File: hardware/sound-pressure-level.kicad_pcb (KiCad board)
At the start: 2 copper layers, 25 x 25 mm, 33 parts, among them P1 CON-SENSOR2, P2 BOOT, P3 DEBUG, U1 XMC1XXX48, U2 DRILL, U3 DRILL, U4 DRILL, U5 DRILL, U6 ICS-43432, X1 16MHz

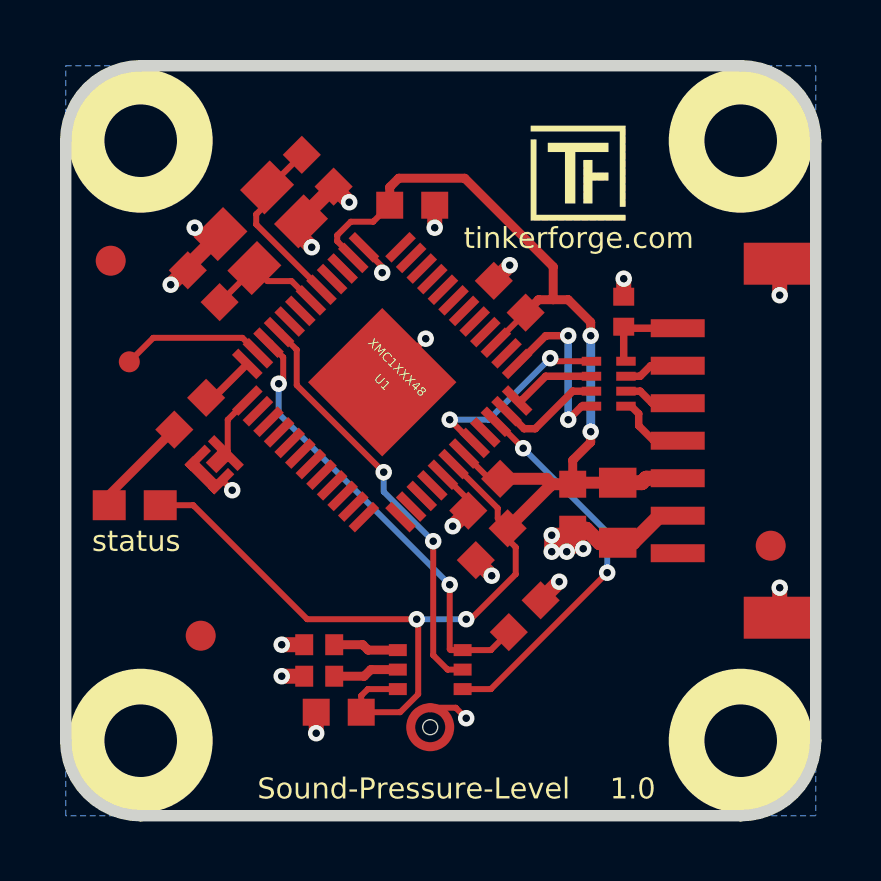
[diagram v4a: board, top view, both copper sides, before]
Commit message: center microphone, pulldown 100k
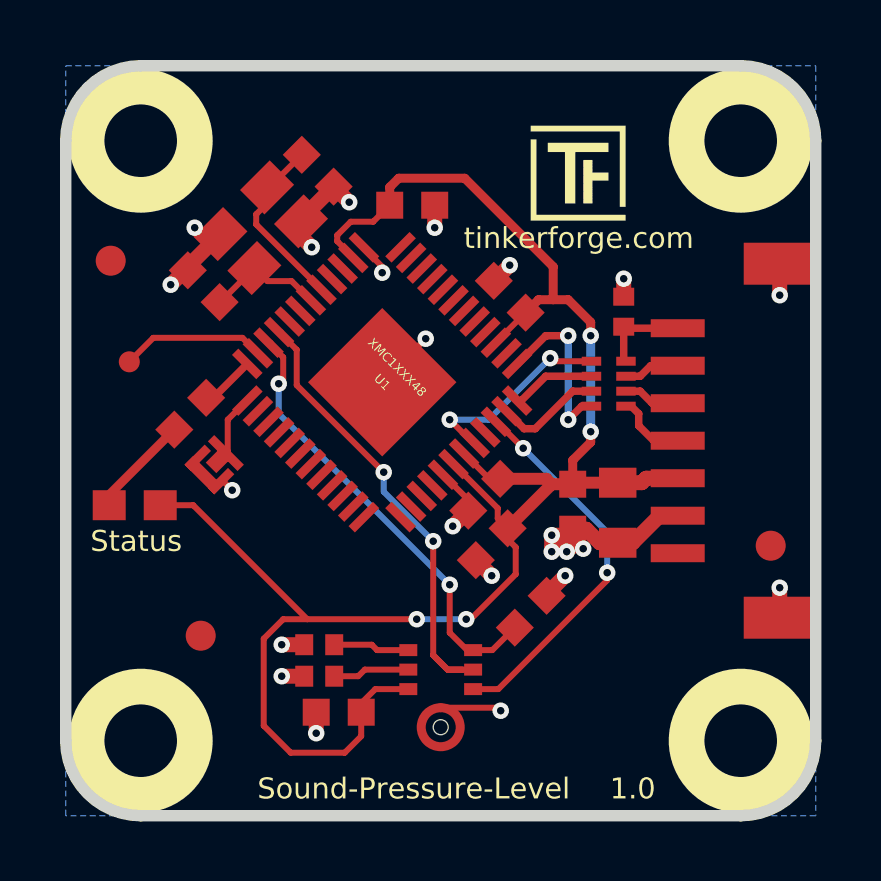
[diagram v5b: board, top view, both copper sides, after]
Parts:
- R2: value 47k -> 100k
- moved U6 0.35 mm to (142.6, 150.6)
- moved R2 0.25 mm to (145.6, 146.7)
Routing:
- net VCC: track 56.5 -> 61.4 mm
- net SCK: track 14.2 -> 15.7 mm
- net GND: track 32.4 -> 33.1 mm
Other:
- board text added: "Status"
- board text removed: "status"
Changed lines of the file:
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@@
-(kicad_pcb (version 4) (host pcbnew 4.0.2+dfsg1-stable)
+(kicad_pcb (version 4) (host pcbnew 4.0.7-e2-6376~58~ubuntu17.04.1)
   (general
     (links 61)
     (no_connects 0)
-    (area 129.909499 128.309499 155.290501 153.690501)
+    (area 13.96714 127.644999 155.955001 196.045)
     (thickness 1.6)
     (drawings 13)
-    (tracks 251)
+    (tracks 257)
     (zones 0)
     (modules 33)
@@
   (layers
     (0 F.Cu signal)
-    (31 B.Cu signal)
+    (31 B.Cu signal hide)
     (32 B.Adhes user)
     (33 F.Adhes user)
@@
     (pad_to_mask_clearance 0)
     (aux_axis_origin 0 0)
-    (visible_elements FFFF7F7F)
+    (visible_elements FFFFFF7F)
     (pcbplotparams
       (layerselection 0x00010_00000000)
@@
   )
   (module kicad-libraries:R0603F (layer F.Cu)
-    (at 145.4 146.85 45)
+    (at 145.6 146.7 45)
     (attr smd)
     (fp_text reference R2 (at 0.05 0.225 45) (layer F.Fab)
       (effects (font (size 0.2 0.2) (thickness 0.05)))
     )
-    (fp_text value 47k (at 0.05 -0.375 45) (layer F.Fab)
+    (fp_text value 100k (at 0.05 -0.375 45) (layer F.Fab)
       (effects (font (size 0.2 0.2) (thickness 0.05)))
     )
@@
   )
   (module kicad-libraries:ICS-43432 (layer F.Cu)
-    (at 142.25 150.55 270)
+    (at 142.6 150.55 270)
     (fp_text reference U6 (at -1.8 0.16 270) (layer F.Fab)
       (effects (font (size 0.15 0.15) (thickness 0.0375)))
@@
     (effects (font (size 0.7 0.7) (thickness 0.15)))
   )
-  (gr_text status (at 132.45 144.35) (layer F.SilkS)
+  (gr_text Status (at 132.45 144.35) (layer F.SilkS)
     (effects (font (size 0.7 0.7) (thickness 0.15)))
   )
@@
   (gr_arc (start 152.6 151) (end 155.1 151) (angle 90) (layer Edge.Cuts) (width 0.381))
   (gr_arc (start 152.6 131) (end 152.6 128.5) (angle 90) (layer Edge.Cuts) (width 0.381))
+  (segment (start 142.6 149.9) (end 144.5 149.9) (width 0.2) (layer F.Cu) (net 1))
+  (via (at 144.6 150) (size 0.55) (drill 0.25) (layers F.Cu B.Cu) (net 1))
+  (segment (start 144.5 149.9) (end 144.6 150) (width 0.2) (layer F.Cu) (net 1))
   (segment (start 134.696447 142.153553) (end 134.696447 142.146447) (width 0.2) (layer F.Cu) (net 1))
   (segment (start 134.696447 142.146447) (end 134.4 141.85) (width 0.2) (layer F.Cu) (net 1))
@@
   (segment (start 138.45 150.05) (end 138.45 150.75) (width 0.5) (layer F.Cu) (net 1))
   (via (at 138.45 150.75) (size 0.55) (drill 0.25) (layers F.Cu B.Cu) (net 1))
-  (segment (start 145.93033 146.31967) (end 146.55 145.7) (width 0.5) (layer F.Cu) (net 1))
-  (via (at 146.55 145.7) (size 0.55) (drill 0.25) (layers F.Cu B.Cu) (net 1))
-  (segment (start 142.25 149.9) (end 143.1 149.9) (width 0.2) (layer F.Cu) (net 1))
-  (via (at 143.45 150.25) (size 0.55) (drill 0.25) (layers F.Cu B.Cu) (net 1))
-  (segment (start 143.1 149.9) (end 143.45 150.25) (width 0.2) (layer F.Cu) (net 1))
+  (segment (start 146.13033 146.11967) (end 146.75 145.5) (width 0.5) (layer F.Cu) (net 1))
+  (via (at 146.75 145.5) (size 0.55) (drill 0.25) (layers F.Cu B.Cu) (net 1))
   (segment (start 146.8 144.15) (end 146.3 144.15) (width 0.5) (layer F.Cu) (net 1))
   (via (at 146.3 144.15) (size 0.55) (drill 0.25) (layers F.Cu B.Cu) (net 1))
@@
   (segment (start 137.943446 133.688066) (end 137.943446 133.617214) (width 0.2) (layer F.Cu) (net 1))
   (segment (start 137.943446 133.617214) (end 139.03033 132.53033) (width 0.5) (layer F.Cu) (net 1))
+  (segment (start 139.95 150.05) (end 139.95 150.85) (width 0.2) (layer F.Cu) (net 2))
+  (segment (start 137.35 146.95) (end 138.15 146.95) (width 0.2) (layer F.Cu) (net 2))
+  (segment (start 136.7 147.6) (end 137.35 146.95) (width 0.2) (layer F.Cu) (net 2))
+  (segment (start 136.7 150.5) (end 136.7 147.6) (width 0.2) (layer F.Cu) (net 2))
+  (segment (start 137.6 151.4) (end 136.7 150.5) (width 0.2) (layer F.Cu) (net 2))
+  (segment (start 139.4 151.4) (end 137.6 151.4) (width 0.2) (layer F.Cu) (net 2))
+  (segment (start 139.95 150.85) (end 139.4 151.4) (width 0.2) (layer F.Cu) (net 2))
+  (segment (start 141.52 149.28) (end 140.42 149.28) (width 0.2) (layer F.Cu) (net 2))
+  (segment (start 140.42 149.28) (end 139.95 149.75) (width 0.2) (layer F.Cu) (net 2))
+  (segment (start 139.95 149.75) (end 139.95 150.05) (width 0.2) (layer F.Cu) (net 2))
   (segment (start 141.8 146.95) (end 138.15 146.95) (width 0.2) (layer F.Cu) (net 2))
   (segment (start 134.35 143.15) (end 133.2501 143.15) (width 0.2) (layer F.Cu) (net 2))
   (segment (start 138.15 146.95) (end 134.35 143.15) (width 0.2) (layer F.Cu) (net 2))
-  (segment (start 139.95 150.05) (end 139.95 149.5) (width 0.2) (layer F.Cu) (net 2))
-  (segment (start 140.17 149.28) (end 141.17 149.28) (width 0.2) (layer F.Cu) (net 2))
-  (segment (start 139.95 149.5) (end 140.17 149.28) (width 0.2) (layer F.Cu) (net 2))
   (segment (start 144.83033 143.91967) (end 144.83033 144.28033) (width 0.2) (layer F.Cu) (net 2))
   (segment (start 144.83033 144.28033) (end 145.1 144.55) (width 0.2) (layer F.Cu) (net 2))
-  (segment (start 141.25 150.05) (end 139.95 150.05) (width 0.2) (layer F.Cu) (net 2))
-  (segment (start 141.85 149.45) (end 141.25 150.05) (width 0.2) (layer F.Cu) (net 2))
-  (segment (start 141.85 147) (end 141.85 149.45) (width 0.2) (layer F.Cu) (net 2))
   (segment (start 141.8 146.95) (end 141.85 147) (width 0.2) (layer F.Cu) (net 2))
   (via (at 141.8 146.95) (size 0.55) (drill 0.25) (layers F.Cu B.Cu) (net 2))
@@
   (segment (start 134.78033 139.56967) (end 135.022361 139.56967) (width 0.25) (layer F.Cu) (net 16))
   (segment (start 135.022361 139.56967) (end 136.152688 138.439343) (width 0.25) (layer F.Cu) (net 16))
-  (segment (start 143.33 147.98) (end 144.27 147.98) (width 0.2) (layer F.Cu) (net 17))
-  (segment (start 144.27 147.98) (end 144.86967 147.38033) (width 0.2) (layer F.Cu) (net 17))
-  (segment (start 143.33 147.98) (end 142.93 147.98) (width 0.2) (layer F.Cu) (net 17))
+  (segment (start 145.06967 147.23033) (end 144.32 147.98) (width 0.2) (layer F.Cu) (net 17))
+  (segment (start 144.32 147.98) (end 143.68 147.98) (width 0.2) (layer F.Cu) (net 17))
+  (segment (start 143.68 147.98) (end 143.48 147.98) (width 0.2) (layer F.Cu) (net 17))
+  (segment (start 143.48 147.98) (end 142.9 147.4) (width 0.2) (layer F.Cu) (net 17))
   (segment (start 137.35 138.221366) (end 136.860332 137.731698) (width 0.2) (layer F.Cu) (net 17))
   (segment (start 137.35 138.95) (end 137.35 138.221366) (width 0.2) (layer F.Cu) (net 17))
@@
   (segment (start 142.9 145.8) (end 137.2 140.1) (width 0.2) (layer B.Cu) (net 17))
   (via (at 142.9 145.8) (size 0.55) (drill 0.25) (layers F.Cu B.Cu) (net 17))
-  (segment (start 142.9 147.95) (end 142.9 145.8) (width 0.2) (layer F.Cu) (net 17))
-  (segment (start 142.93 147.98) (end 142.9 147.95) (width 0.2) (layer F.Cu) (net 17))
+  (segment (start 142.9 147.4) (end 142.9 145.8) (width 0.2) (layer F.Cu) (net 17))
   (segment (start 136.931698 137.731698) (end 136.860332 137.731698) (width 0.2) (layer F.Cu) (net 17))
   (segment (start 136.881698 137.731698) (end 136.860332 137.731698) (width 0.2) (layer F.Cu) (net 17))
-  (segment (start 143.33 147.98) (end 143.42 147.98) (width 0.3) (layer F.Cu) (net 17))
+  (segment (start 143.68 149.28) (end 144.52 149.28) (width 0.2) (layer F.Cu) (net 34))
+  (segment (start 148.15 145.65) (end 148.15 145.4) (width 0.2) (layer F.Cu) (net 34))
+  (segment (start 144.52 149.28) (end 148.15 145.65) (width 0.2) (layer F.Cu) (net 34))
   (segment (start 144.439668 140.368302) (end 144.468302 140.368302) (width 0.2) (layer F.Cu) (net 34))
   (segment (start 144.468302 140.368302) (end 145.35 141.25) (width 0.2) (layer F.Cu) (net 34))
@@
   (segment (start 148.15 144.05) (end 148.15 145.4) (width 0.2) (layer B.Cu) (net 34))
   (via (at 148.15 145.4) (size 0.55) (drill 0.25) (layers F.Cu B.Cu) (net 34))
-  (segment (start 148.15 145.4) (end 144.27 149.28) (width 0.2) (layer F.Cu) (net 34))
-  (segment (start 144.27 149.28) (end 143.33 149.28) (width 0.2) (layer F.Cu) (net 34))
+  (segment (start 143.68 148.63) (end 142.83 148.63) (width 0.2) (layer F.Cu) (net 49))
+  (segment (start 142.83 148.63) (end 142.35 148.15) (width 0.2) (layer F.Cu) (net 49))
   (segment (start 143.33 148.63) (end 142.83 148.63) (width 0.2) (layer F.Cu) (net 49))
   (segment (start 137.8 137.967314) (end 137.212358 137.379672) (width 0.2) (layer F.Cu) (net 49))
@@
   (segment (start 137.279672 137.379672) (end 137.212358 137.379672) (width 0.2) (layer F.Cu) (net 49))
   (segment (start 137.212358 137.412358) (end 137.212358 137.379672) (width 0.2) (layer F.Cu) (net 49))
-  (segment (start 139.05 147.8) (end 140 147.8) (width 0.3) (layer F.Cu) (net 50))
-  (segment (start 140.18 147.98) (end 141.17 147.98) (width 0.3) (layer F.Cu) (net 50))
-  (segment (start 140 147.8) (end 140.18 147.98) (width 0.3) (layer F.Cu) (net 50))
-  (segment (start 141.17 148.63) (end 140.27 148.63) (width 0.3) (layer F.Cu) (net 51))
-  (segment (start 140.05 148.85) (end 139.05 148.85) (width 0.3) (layer F.Cu) (net 51))
-  (segment (start 140.27 148.63) (end 140.05 148.85) (width 0.3) (layer F.Cu) (net 51))
+  (segment (start 141.52 147.98) (end 140.48 147.98) (width 0.2) (layer F.Cu) (net 50))
+  (segment (start 140.3 147.8) (end 139.05 147.8) (width 0.2) (layer F.Cu) (net 50))
+  (segment (start 140.48 147.98) (end 140.3 147.8) (width 0.2) (layer F.Cu) (net 50))
+  (segment (start 141.52 148.63) (end 140.07 148.63) (width 0.2) (layer F.Cu) (net 51))
+  (segment (start 139.85 148.85) (end 139.05 148.85) (width 0.2) (layer F.Cu) (net 51))
+  (segment (start 140.07 148.63) (end 139.85 148.85) (width 0.2) (layer F.Cu) (net 51))
   (segment (start 136.50651 138.08552) (end 136.50552 138.08552) (width 0.2) (layer F.Cu) (net 52))
   (segment (start 136.50552 138.08552) (end 135.99 137.57) (width 0.2) (layer F.Cu) (net 52))
@@
     (polygon
       (pts
-        (xy 155.1 153.5) (xy 130.1 153.5) (xy 130.1 128.5) (xy 155.1 128.5) (xy 155.1 153.5)
+        (xy 155.1 153.5) (xy 130.1 153.5) (xy 130.1 128.5) (xy 155.1 128.5)
       )
     )
